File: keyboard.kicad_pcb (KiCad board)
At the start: 2 copper layers, 323.7 x 193.9 mm, 155 parts, among them P1 USB_OTG, P10 CONN_01X01, P11 CONN_01X01, P12 CONN_01X01, P13 CONN_01X01, P15 CONN_01X06, P16 CONN_01X06, P17 CONN_01X01, P18 CONN_01X06, P2 CONN_02X03, P3 CONN_01X01, P4 CONN_01X01, P5 CONN_01X01, P6 CONN_01X01, P7 CONN_01X01, P8 CONN_01X01, P9 CONN_01X01, SW1 SW_PUSH, SW10 SW_PUSH, SW11 SW_PUSH, SW12 SW_PUSH, SW13 SW_PUSH, SW14 SW_PUSH, SW15 SW_PUSH, SW16 SW_PUSH, SW2 SW_PUSH, SW24 SW_PUSH, SW25 SW_PUSH, SW26 SW_PUSH, SW27 SW_PUSH, SW28 SW_PUSH, SW29 SW_PUSH, SW3 SW_PUSH, SW30 SW_PUSH, SW31 SW_PUSH, SW32 SW_PUSH, SW33 SW_PUSH, SW34 SW_PUSH, SW35 SW_PUSH, SW36 SW_PUSH, SW37 SW_PUSH, SW4 SW_PUSH, SW5 SW_PUSH, SW6 SW_PUSH, SW7 SW_PUSH, SW8 SW_PUSH, SW9 SW_PUSH, U1 ATmega32U4, X1 CRYSTAL_SMD

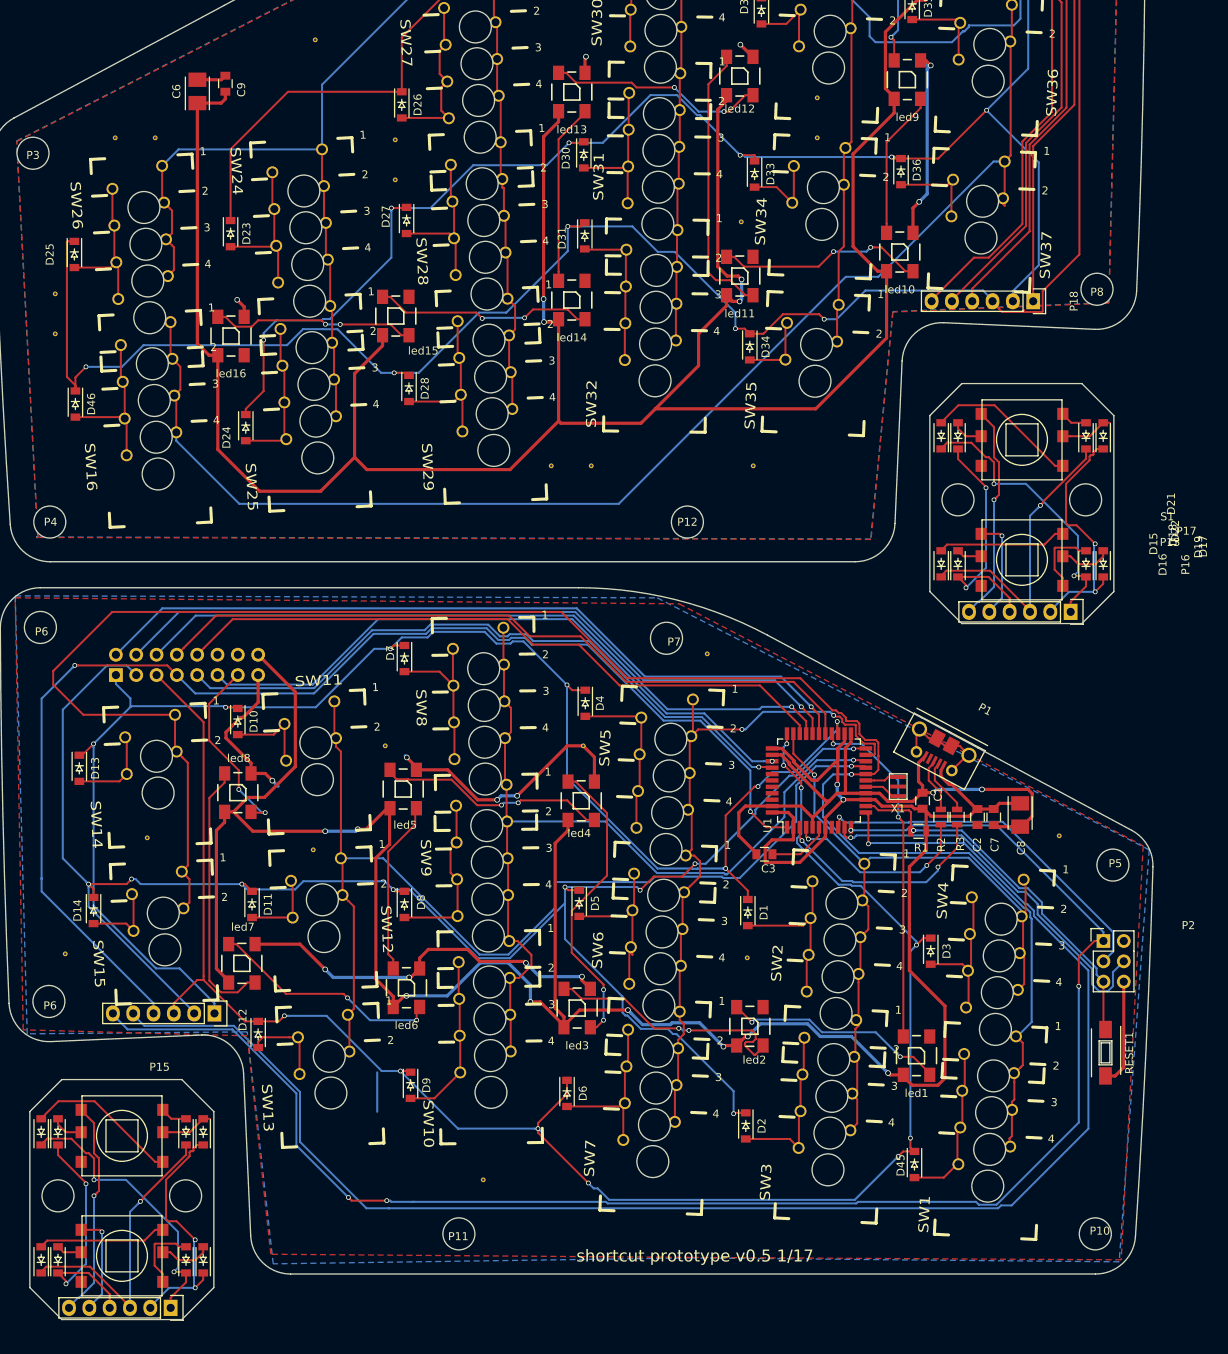
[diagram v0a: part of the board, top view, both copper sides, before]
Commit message: fixed: silks, fids, col2 via, serial patches
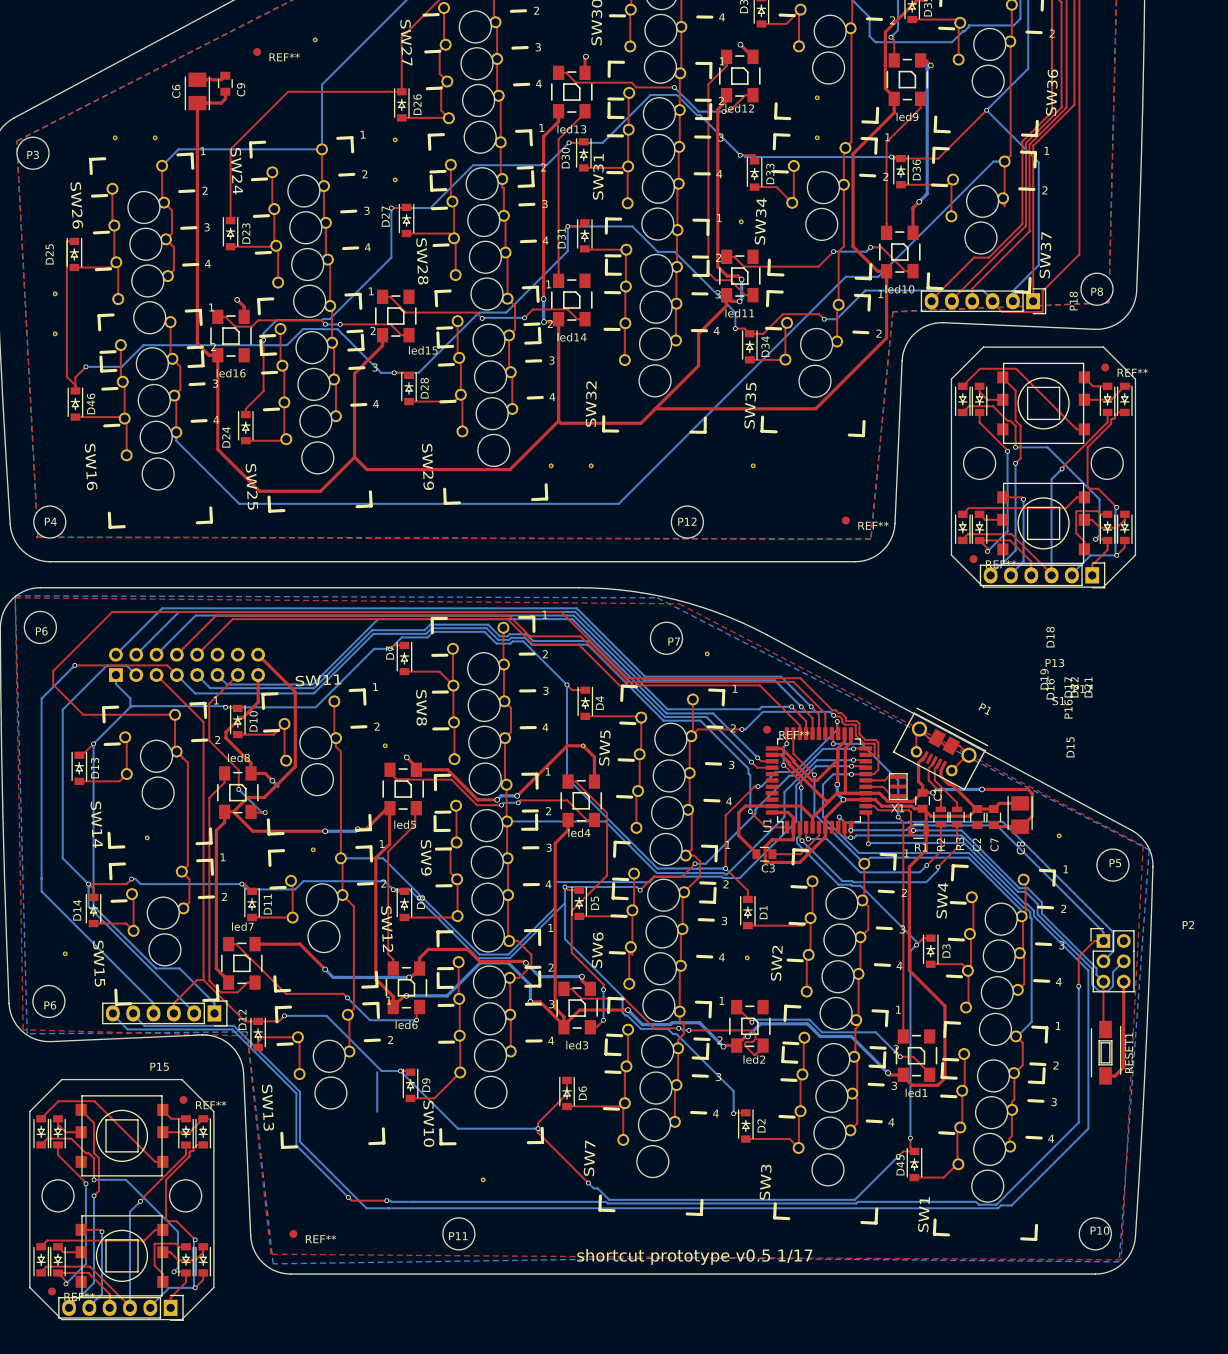
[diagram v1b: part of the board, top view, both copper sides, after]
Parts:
- added REF**: Fiducial_1mm_Dia_2.54mm_Outer_CopperTop, Fiducials:Fiducial_1mm_Dia_2.54mm_Outer_CopperTop, F.Cu at (161.0, 64.5)
- added REF**: Fiducial_1mm_Dia_2.54mm_Outer_CopperTop, Fiducials:Fiducial_1mm_Dia_2.54mm_Outer_CopperTop, F.Cu at (144.6, 88.4)
- added REF**: Fiducial_1mm_Dia_2.54mm_Outer_CopperTop, Fiducials:Fiducial_1mm_Dia_2.54mm_Outer_CopperTop, F.Cu at (55.0, 25.0)
- added REF**: Fiducial_1mm_Dia_2.54mm_Outer_CopperTop, Fiducials:Fiducial_1mm_Dia_2.54mm_Outer_CopperTop, F.Cu at (128.6, 83.6)
- added REF**: Fiducial_1mm_Dia_2.54mm_Outer_CopperTop, Fiducials:Fiducial_1mm_Dia_2.54mm_Outer_CopperTop, F.Cu at (59.5, 172.8)
- added REF**: Fiducial_1mm_Dia_2.54mm_Outer_CopperTop, Fiducials:Fiducial_1mm_Dia_2.54mm_Outer_CopperTop, F.Cu at (118.7, 109.7)
- added REF**: Fiducial_1mm_Dia_2.54mm_Outer_CopperTop, Fiducials:Fiducial_1mm_Dia_2.54mm_Outer_CopperTop, F.Cu at (29.4, 180.0)
- added REF**: Fiducial_1mm_Dia_2.54mm_Outer_CopperTop, Fiducials:Fiducial_1mm_Dia_2.54mm_Outer_CopperTop, F.Cu at (45.8, 156.0)
- moved D15 5.30 mm to (161.3, 84.4)
- moved D18 5.30 mm to (145.3, 84.4)
- moved D21 5.30 mm to (161.3, 68.4)
- moved D22 5.30 mm to (145.3, 68.4)
- moved P17 5.30 mm to (145.3, 76.4)
- moved S1 5.30 mm to (153.3, 83.9)
- moved S2 5.30 mm to (153.3, 68.9)
- moved D16 5.30 mm to (163.4, 84.4)
- moved D17 5.30 mm to (143.2, 84.4)
- moved D19 5.30 mm to (143.2, 68.4)
- moved D20 5.30 mm to (163.4, 68.4)
- moved P13 5.30 mm to (161.2, 76.4)
- moved P16 5.30 mm to (159.4, 90.4)
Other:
- outline, holes or cut-outs redrawn
- board text added: "serial"

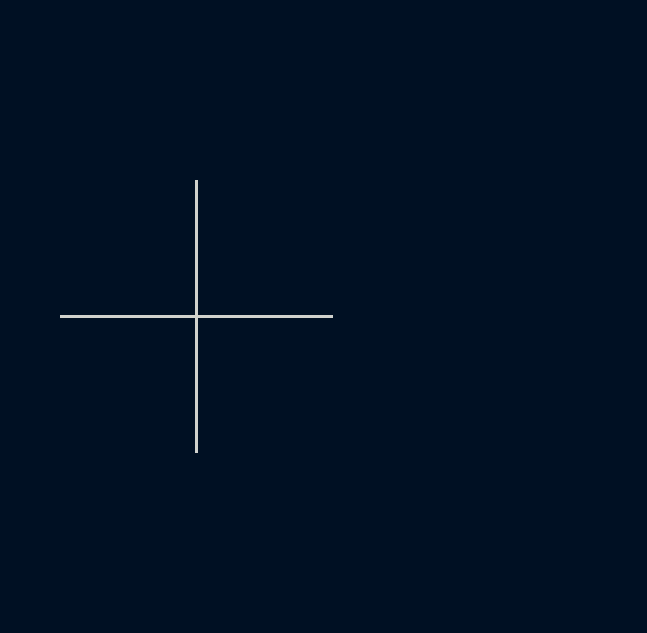
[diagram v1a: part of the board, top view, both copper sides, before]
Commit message: removed silk cross
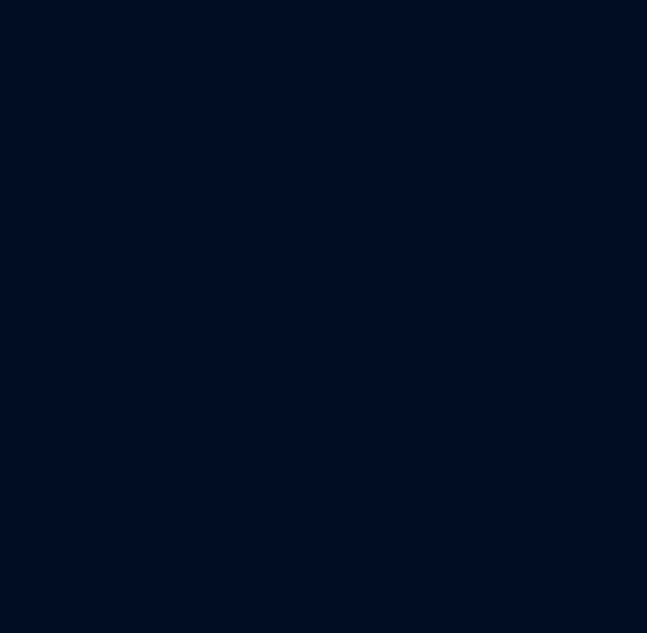
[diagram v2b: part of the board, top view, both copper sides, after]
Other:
- board size 323.7 x 193.9 mm -> 145 x 180.5 mm

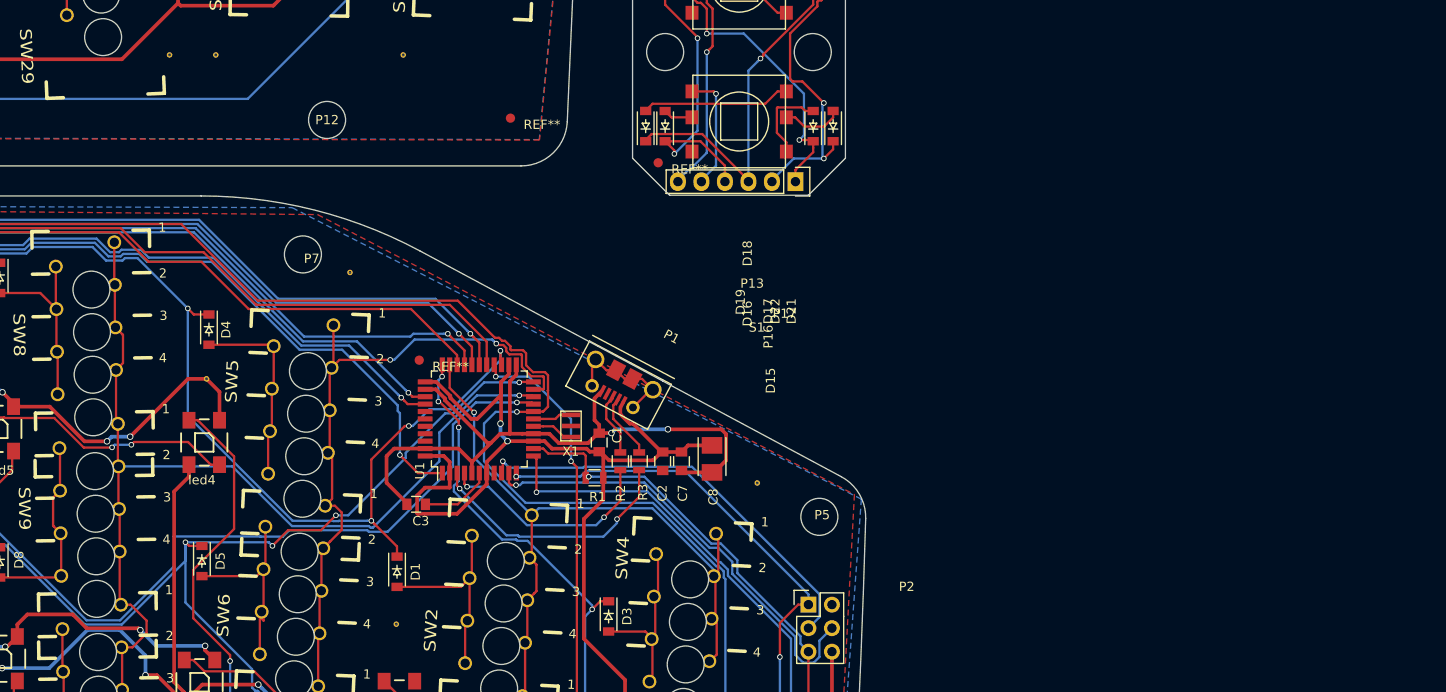
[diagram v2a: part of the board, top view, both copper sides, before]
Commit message: added hwb resistor
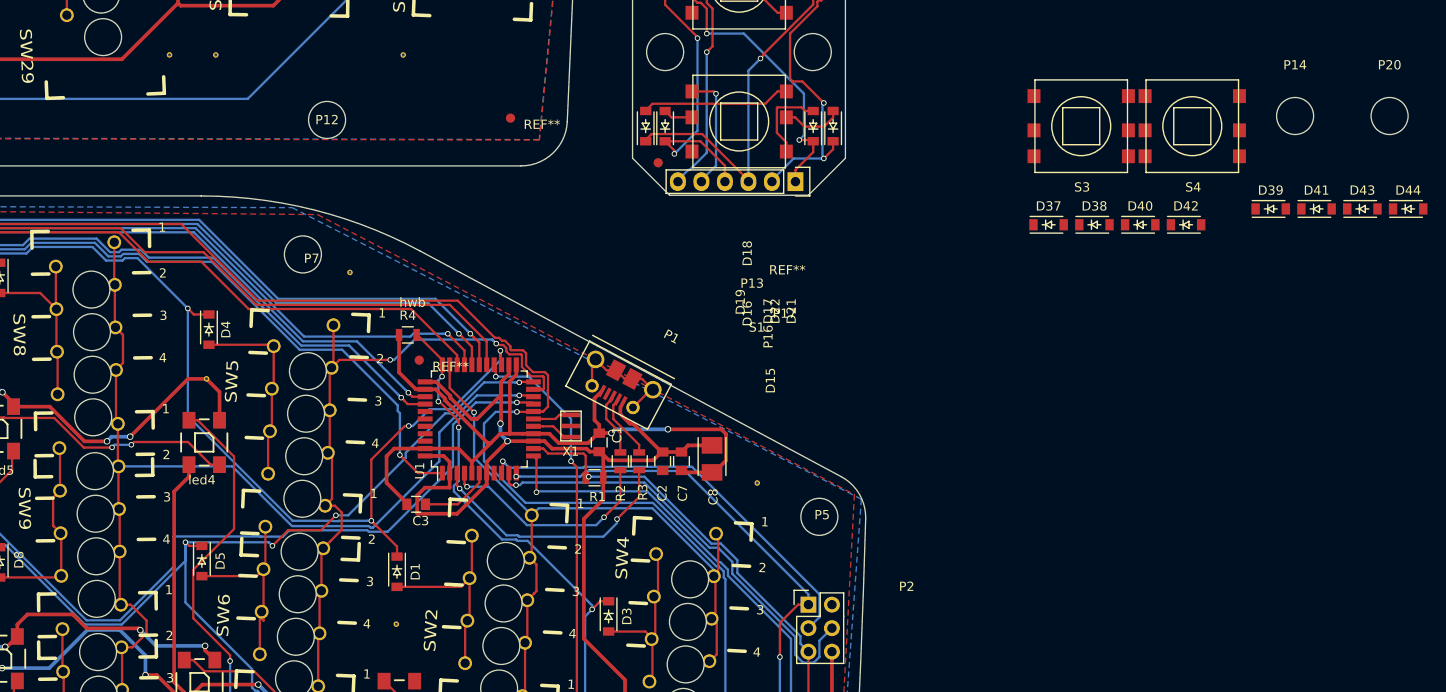
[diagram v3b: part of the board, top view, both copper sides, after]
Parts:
- added D37: D, Diodes_SMD:SOD-123, F.Cu at (186.7, 95.1)
- added D38: D, Diodes_SMD:SOD-123, F.Cu at (191.7, 95.1)
- added D39: D, Diodes_SMD:SOD-123, F.Cu at (210.7, 93.4)
- added D40: D, Diodes_SMD:SOD-123, F.Cu at (196.6, 95.1)
- added D41: D, Diodes_SMD:SOD-123, F.Cu at (215.7, 93.4)
- added D42: D, Diodes_SMD:SOD-123, F.Cu at (201.6, 95.1)
- added D43: D, Diodes_SMD:SOD-123, F.Cu at (220.6, 93.4)
- added D44: D, Diodes_SMD:SOD-123, F.Cu at (225.6, 93.4)
- added P14: CONN_01X01, Mounting_Holes:MountingHole_4mm, F.Cu at (213.4, 83.3)
- added P20: CONN_01X01, Mounting_Holes:MountingHole_4mm, F.Cu at (223.6, 83.3)
- added R4: 10k, Resistors_SMD:R_0805, F.Cu at (117.5, 107.0)
- added S3: alps_4way, fp:alps 4way smt, F.Cu at (190.3, 84.4)
- added S4: alps_4way, fp:alps 4way smt, F.Cu at (202.3, 84.4)
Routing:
- net Earth: track 226.3 -> 234.0 mm
- net /row3: track 223.6 -> 228.0 mm
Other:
- board text added: "hwb"

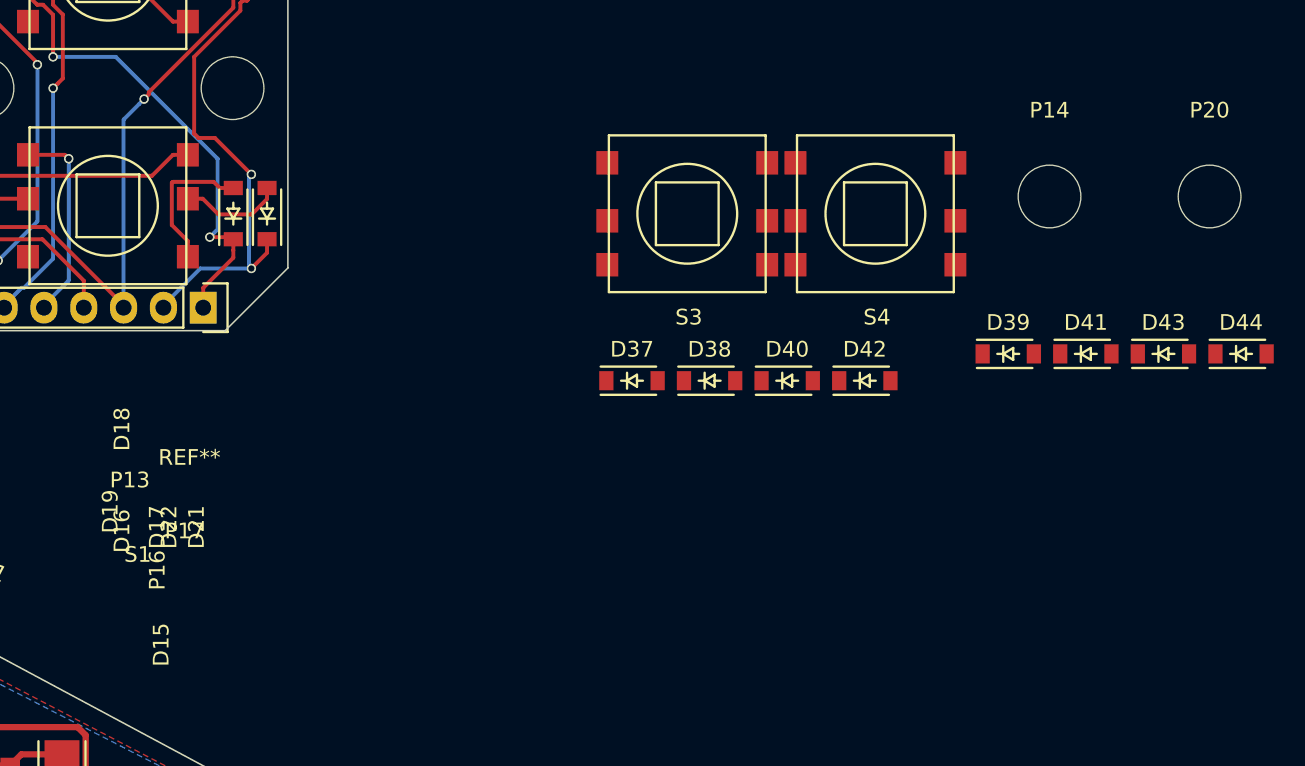
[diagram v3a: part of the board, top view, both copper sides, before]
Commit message: redid thumboard components
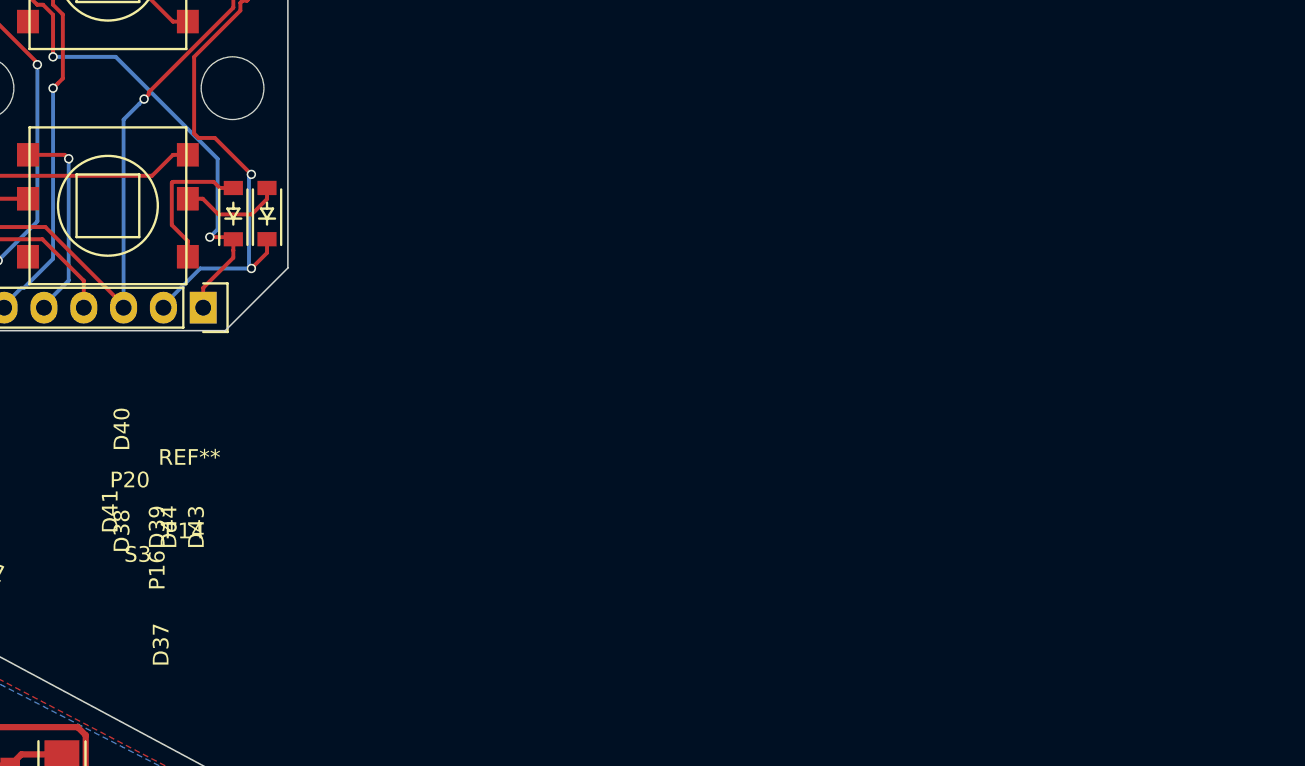
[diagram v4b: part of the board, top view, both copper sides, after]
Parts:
- removed the D37 at (186.7, 95.1)
- removed the D38 at (191.7, 95.1)
- removed the D39 at (210.7, 93.4)
- removed the D40 at (196.6, 95.1)
- removed the D41 at (215.7, 93.4)
- removed the D42 at (201.6, 95.1)
- removed the D43 at (220.6, 93.4)
- removed the D44 at (225.6, 93.4)
- removed the P14 at (213.4, 83.3)
- removed the P20 at (223.6, 83.3)
- removed the S3 at (190.3, 84.4)
- removed the S4 at (202.3, 84.4)
- renumbered D15 to D37, D16 to D38, D17 to D39, D18 to D40, D19 to D41, D20 to D42, D21 to D43, D22 to D44, P17 to P14, P13 to P20, S1 to S3, S2 to S4
